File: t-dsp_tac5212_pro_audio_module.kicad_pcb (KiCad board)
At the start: 4 copper layers, 42 x 26.5 mm, 110 parts, among them J3V108 jumper, J5V108 jumper, T108 Tab, T109 Tab, T110 Tab, T111 Tab, U108 Single Buffer with Tri-state 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, U109 3.3v LDO - TLV74133PDBVR

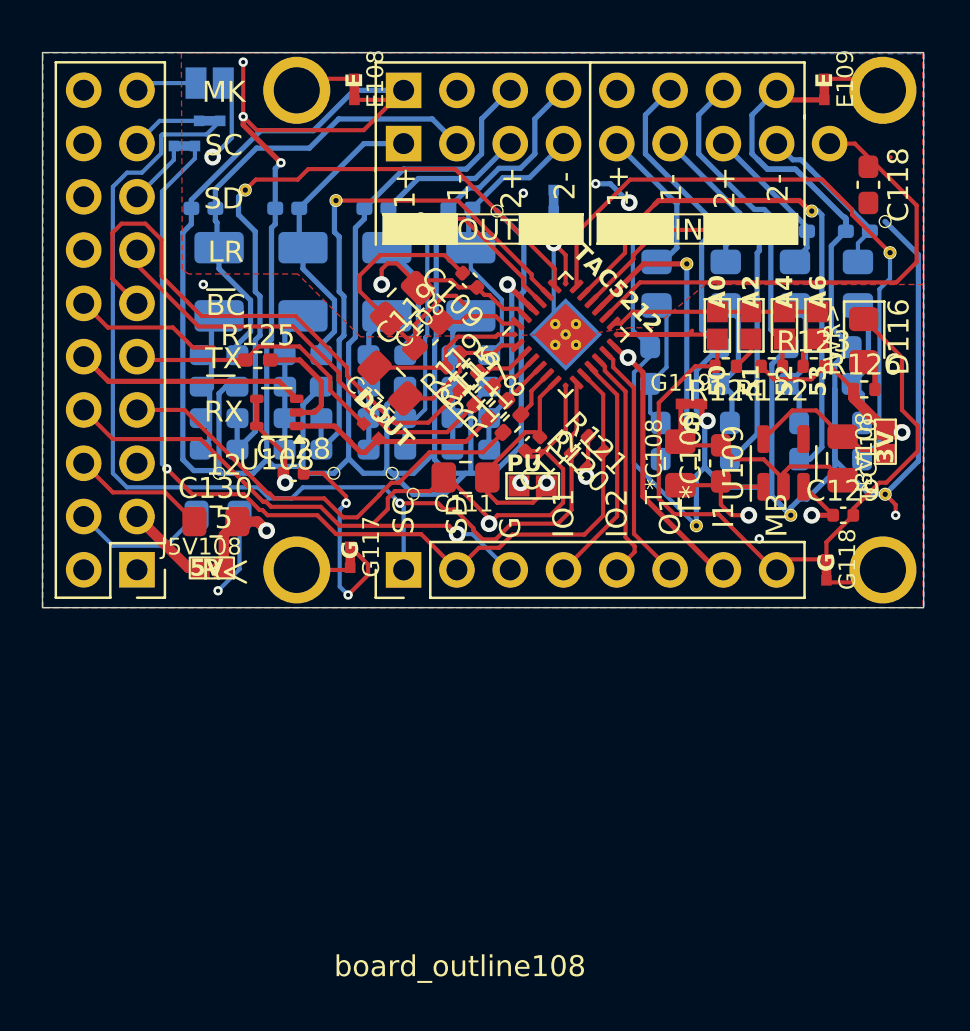
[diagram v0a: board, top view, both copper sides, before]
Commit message: Add 3D renders, hide ref designators, fix legacy 3D model paths
- Add Blender 3D render output (8 views: top, bottom, 4 sides, 2 isometric)
  to KiBot config and manufacturing ZIP
- Split CI workflow into 3 steps: manufacturing outputs, 3D renders
  (kicad9_auto_full), and ZIP packaging
- Add PCB spec report to manufacturing outputs
- Hide reference designators and component values from silkscreen
- Replace legacy ${KISYS3DMOD} with ${KICAD9_3DMODEL_DIR} across all
  footprint libraries and PCB (47 files)
- Add new 3D models (TPD1E10B06, VQFN-24) and footprints
- Set net tie footprint type on jumper components

Co-Authored-By: Claude Opus 4.6 <noreply@anthropic.com>
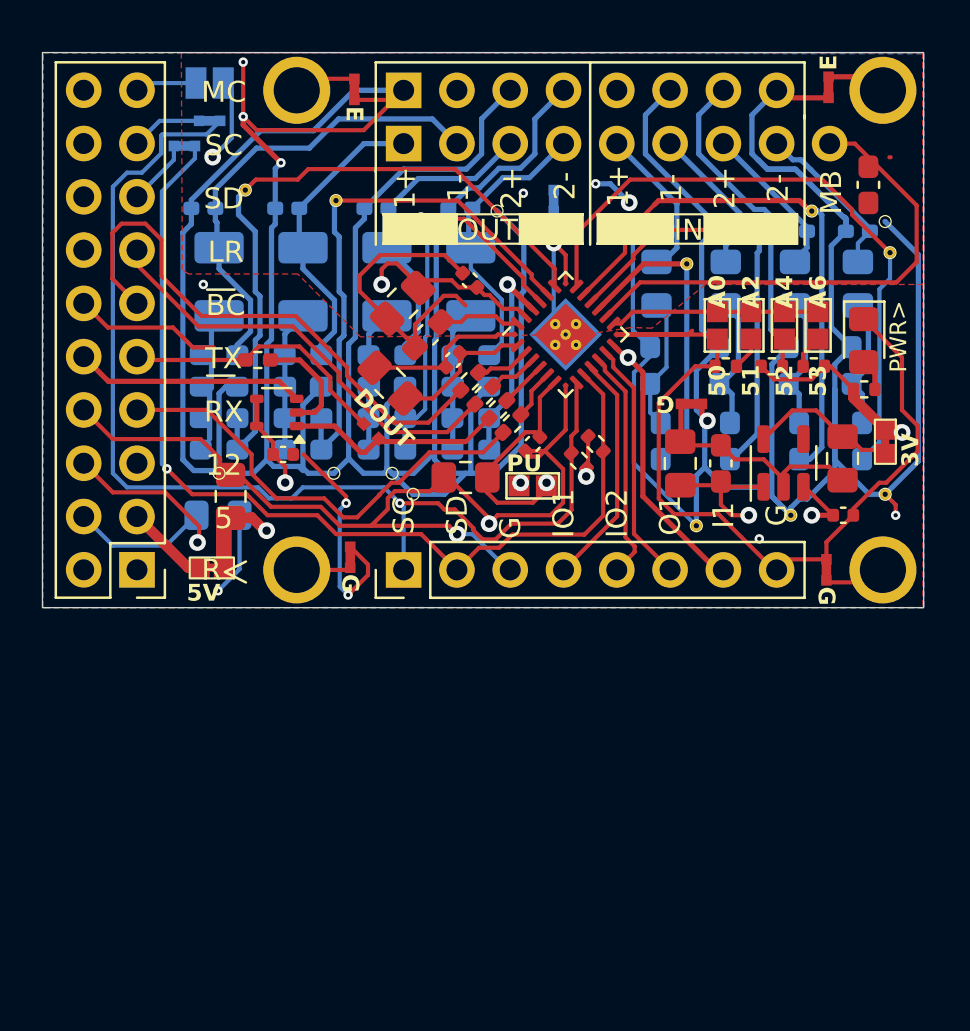
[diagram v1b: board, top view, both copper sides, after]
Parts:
- C113, C114, C120, C122: footprint Capacitor_SMD:C_0603_1608Metric_Pad1.08x0.95mm_HandSolder -> project_fp:C_0603_1608Metric_Pad1.08x0.95mm_HandSolder
- G119: footprint project_fp:jumper_slice_alt1 -> project_fp:jumper_slice
- MCLK108: footprint Jumper:SolderJumper-2_P1.3mm_Open_Pad1.0x1.5mm -> project_fp:SolderJumper-2_P1.3mm_Open_Pad1.0x1.5mm_Master_Clock
- T108, T109, T110, T111: footprint kikit:Tab -> project_fp:Tab
- U108: footprint Package_TO_SOT_SMD:SOT-353_SC-70-5 -> project_fp:SOT-353_SC-70-5
- moved C130 1.39 mm to (93.8, 119.1), turned to 90 degrees
- moved C128 1.03 mm to (96.3, 117.1)
- moved E109 0.22 mm to (122.3, 99.6), turned to -90 degrees
- turned G119 to 0 degrees
- turned GND108 to 90 degrees
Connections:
- E109 pad 1: Earth -> Net-(E109-Pad1)
- E109 pad 2: Net-(E109-Pad2) -> Earth
- G119 pad 1: Earth -> Net-(U109-GND)
- G119 pad 2: Net-(U109-GND) -> Earth
- GND108 pad 1: Earth -> GNDD
- GND108 pad 2: GNDD -> Earth
- board_outline108 pad 50: Net-(E109-Pad2) -> Net-(E109-Pad1)
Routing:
- net Net-(E109-Pad2): track 3.02 -> 0.00 mm
- net Net-(E109-Pad1): track 0.00 -> 2.86 mm
- net GNDD: track 167.6 -> 170.0 mm, vias 7 -> 8
- net Earth: track 297.5 -> 295.2 mm
- net 5212_DIN1: track 21.3 -> 21.8 mm
